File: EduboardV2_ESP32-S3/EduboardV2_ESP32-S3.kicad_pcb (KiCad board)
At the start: 4 copper layers, 35 x 63.3 mm, 22 parts, among them J1 EduboardV2 PCIE UP Board Conn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, Q3 AO3401A, SW1 K2-1102SP-C4SC-04, U1 ESP32-S3-WROOM-1(N8R2), U5 LD1117S33TR_SOT223

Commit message: finish schematic. Do Layout
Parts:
- removed C17: 100n, Capacitor_SMD:C_0603_1608Metric
- removed R19: 10k, Resistor_SMD:R_0603_1608Metric
- removed R29, R30: 0R, Resistor_SMD:R_0603_1608Metric
- added C1: 100n, Capacitor_SMD:C_0603_1608Metric, F.Cu at (133.2, 118.9)
- added C2: 4u7, Capacitor_SMD:C_0805_2012Metric, F.Cu at (133.0, 117.1)
- added C3: 1u, Capacitor_SMD:C_0805_2012Metric, F.Cu at (129.1, 117.5)
- added C4: 4u7, Capacitor_SMD:C_0805_2012Metric, F.Cu at (117.4, 111.2)
- added C5: 100n, Capacitor_SMD:C_0603_1608Metric, F.Cu at (119.2, 111.5)
- added C6: 1u, Capacitor_SMD:C_0805_2012Metric, F.Cu at (117.4, 114.7)
- added JP1: SolderJumper_2_Bridged, Jumper:SolderJumper-2_P1.3mm_Bridged_RoundedPad1.0x1.5mm, B.Cu at (122.1, 137.9)
- added JP10: SolderJumper_3_Bridged12, EduboardV2_kicadlib:SolderJumper_Small-3_bridged12, B.Cu at (127.0, 141.3)
- added JP11: SolderJumper_3_Bridged12, EduboardV2_kicadlib:SolderJumper_Small-3_bridged12, B.Cu at (120.8, 141.3)
- added JP12: SolderJumper_3_Bridged12, EduboardV2_kicadlib:SolderJumper_Small-3_bridged12, B.Cu at (117.7, 141.3)
- added JP2: SolderJumper_2_Bridged, Jumper:SolderJumper-2_P1.3mm_Bridged_RoundedPad1.0x1.5mm, B.Cu at (119.5, 137.9)
- added JP3: SolderJumper_2_Bridged, Jumper:SolderJumper-2_P1.3mm_Bridged_RoundedPad1.0x1.5mm, B.Cu at (116.9, 137.9)
- added JP4: SolderJumper_3_Bridged12, EduboardV2_kicadlib:SolderJumper_Small-3_bridged12, B.Cu at (123.9, 141.3)
- added JP5: SolderJumper_3_Bridged12, EduboardV2_kicadlib:SolderJumper_Small-3_bridged12, B.Cu at (130.8, 124.2)
- added JP6: SolderJumper_3_Bridged12, EduboardV2_kicadlib:SolderJumper_Small-3_bridged12, B.Cu at (133.9, 124.2)
- added JP7: SolderJumper_3_Bridged12, EduboardV2_kicadlib:SolderJumper_Small-3_bridged12, B.Cu at (127.7, 124.2)
- added JP8: SolderJumper_3_Bridged12, EduboardV2_kicadlib:SolderJumper_Small-3_bridged12, B.Cu at (124.6, 124.2)
- added JP9: SolderJumper_3_Bridged12, EduboardV2_kicadlib:SolderJumper_Small-3_bridged12, B.Cu at (130.1, 141.3)
- added Q1: L8050QLT1G, EduboardV2_kicadlib:SOT-23-3_L2.9-W1.3-P1.90-LS2.4-BR, F.Cu at (110.6, 123.9)
- added Q2: L8050QLT1G, EduboardV2_kicadlib:SOT-23-3_L2.9-W1.3-P1.90-LS2.4-BR, F.Cu at (110.6, 120.2)
- added R1: 2k2, Resistor_SMD:R_0402_1005Metric, F.Cu at (119.0, 116.5)
- added R10: 0R, Resistor_SMD:R_0402_1005Metric, F.Cu at (129.0, 115.0)
- added R11: 10k, Resistor_SMD:R_0402_1005Metric, F.Cu at (112.9, 122.4)
- added R12: 10k, Resistor_SMD:R_0402_1005Metric, F.Cu at (112.9, 119.3)
- added R13: 0R, Resistor_SMD:R_0402_1005Metric, F.Cu at (108.3, 124.0)
- added R14: 0R, Resistor_SMD:R_0402_1005Metric, F.Cu at (108.3, 121.2)
- added R2: 10k, Resistor_SMD:R_0402_1005Metric, F.Cu at (130.7, 118.2)
- added R3: 22k, Resistor_SMD:R_0402_1005Metric, F.Cu at (115.4, 115.7)
- added R4: 47k, Resistor_SMD:R_0402_1005Metric, F.Cu at (119.0, 114.0)
- added R8: 10k, Resistor_SMD:R_0402_1005Metric, F.Cu at (120.0, 116.5)
- added R9: 0R, Resistor_SMD:R_0402_1005Metric, F.Cu at (129.0, 114.0)
- added SW2: K2-1102SP-C4SC-04, EduboardV2_kicadlib:KEY-SMD_4P-L6.0-W6.0-P4.50-LS9.5-BL, F.Cu at (104.7, 116.5)
- added U2: CP2102N-A02-GQFN28R, EduboardV2_kicadlib:QFN-28_L5.0-W5.0-P0.50-TL-EP3.3, F.Cu at (123.6, 114.8)
- R25, R31, R32, R6, R7: footprint Resistor_SMD:R_0603_1608Metric -> Resistor_SMD:R_0402_1005Metric
- moved SW1 65.6 mm to (104.7, 128.7), turned to 180 degrees
- moved C27 51.5 mm to (108.2, 108.6), turned to 90 degrees
- moved Q3 47.3 mm to (111.1, 108.9), turned to -90 degrees
- moved C25 44.1 mm to (115.0, 99.4), turned to 90 degrees
- moved U5 43.2 mm to (107.8, 103.2), turned to 180 degrees
- moved D1 41.1 mm to (116.8, 99.2), turned to 90 degrees
- moved C28 38.0 mm to (106.4, 108.6), turned to 90 degrees
- moved D3 35.0 mm to (122.4, 107.5)
- moved R25 33.9 mm to (109.7, 111.3), turned to 180 degrees
- moved D2 32.2 mm to (124.9, 107.5), turned to 180 degrees
- moved C26 30.3 mm to (113.2, 99.4), turned to 90 degrees
- moved USBC1 27.6 mm to (123.6, 98.4), turned to 180 degrees
- moved R6 22.3 mm to (121.1, 103.0), turned to 180 degrees
- moved R31 21.2 mm to (123.1, 109.2), turned to -90 degrees
- moved R32 21.2 mm to (124.1, 109.2), turned to -90 degrees
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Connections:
- J1 pad 10: USB_Debug_D- -> ESP_D-
- J1 pad 11: unconnected-(J1-UART0_UP_RX-Pad11) -> ESP_U1_RX
- J1 pad 12: USB_Debug_D+ -> ESP_D+
- J1 pad 13: unconnected-(J1-UART1_RS485_TX-Pad13) -> ESP_U2_TX
- J1 pad 15: unconnected-(J1-UART1_RS485_RX-Pad15) -> ESP_U2_RX
- J1 pad 16: unconnected-(J1-RS485_DE-Pad16) -> GPIO_RS485_DE
- J1 pad 17: unconnected-(J1-~{FLASH_CS}-Pad17) -> GPIO_FLASH_CS
- J1 pad 18: unconnected-(J1-~{General_Reset}-Pad18) -> ~{GPIO_General_Reset}
- J1 pad 19: unconnected-(J1-~{SD_CS}-Pad19) -> GPIO_SD_CS
- J1 pad 20: unconnected-(J1-~{TFT_CS}-Pad20) -> GPIO_TFT_CS
- J1 pad 22: unconnected-(J1-TFT_DC-Pad22) -> GPIO_TFT_DC
- J1 pad 24: unconnected-(J1-SPI_SCK-Pad24) -> GPIO_SCK
- J1 pad 26: unconnected-(J1-SPI_MISO-Pad26) -> GPIO_MISO
- J1 pad 28: unconnected-(J1-SPI_MOSI-Pad28) -> GPIO_MOSI
- J1 pad 29: unconnected-(J1-WS2812_Data-Pad29) -> GPIO_WS2812_Data
- J1 pad 30: unconnected-(J1-SCL-Pad30) -> GPIO_SCL
- J1 pad 32: unconnected-(J1-SDA-Pad32) -> GPIO_SDA
- J1 pad 34: unconnected-(J1-GPIOX4/AN5/I2S_MCLK-Pad34) -> ESP_GPIO0
- J1 pad 36: unconnected-(J1-GPIOX3/AN4/I2S_SCLK-Pad36) -> GPIOX3
- J1 pad 38: unconnected-(J1-GPIOX2/AN3/I2S_LRCK-Pad38) -> GPIOX2
- J1 pad 40: unconnected-(J1-GPIOX1/AN2/I2S_DIN-Pad40) -> GPIOX1
- J1 pad 42: unconnected-(J1-GPIOX0/AN1/I2S_DOUT-Pad42) -> GPIOX0
- J1 pad 44: unconnected-(J1-AN0/Pot0-Pad44) -> GPIO_AN0
- J1 pad 46: unconnected-(J1-SW0-Pad46) -> GPIO_SW0
- J1 pad 48: unconnected-(J1-SW1-Pad48) -> GPIO_SW1
- J1 pad 50: unconnected-(J1-SW2-Pad50) -> GPIO_SW2
- J1 pad 52: unconnected-(J1-SW3-Pad52) -> GPIO_SW3
- J1 pad 9: unconnected-(J1-UART0_UP_TX-Pad9) -> ESP_U1_TX
- R31 pad 2: /DebugChip/D_N -> D_N
- R32 pad 2: /DebugChip/D_P -> D_P
- SW1 pad 1: UP_Reset -> ESP_EN
- SW1 pad 2: UP_Reset -> ESP_EN
- U1 pad 1: unconnected-(U1-GND-Pad1) -> GND
- U1 pad 10: unconnected-(U1-IO17-Pad10) -> ESP_U1_TX
- U1 pad 11: unconnected-(U1-IO18-Pad11) -> ESP_U1_RX
- U1 pad 12: unconnected-(U1-IO8-Pad12) -> ~{GPIO_General_Reset}
- U1 pad 13: unconnected-(U1-IO19-Pad13) -> ESP_D-
- U1 pad 14: unconnected-(U1-IO20-Pad14) -> ESP_D+
- U1 pad 15: unconnected-(U1-IO3-Pad15) -> GPIO_FLASH_CS
- U1 pad 16: unconnected-(U1-IO46-Pad16) -> GPIO_Buzzer
- U1 pad 17: unconnected-(U1-IO9-Pad17) -> GPIO_AN0
- U1 pad 18: unconnected-(U1-IO10-Pad18) -> GPIO_SD_CS
- U1 pad 19: unconnected-(U1-IO11-Pad19) -> GPIO_TFT_CS
- U1 pad 2: unconnected-(U1-3V3-Pad2) -> +3V3
- U1 pad 20: unconnected-(U1-IO12-Pad20) -> GPIO_MISO
- U1 pad 21: unconnected-(U1-IO13-Pad21) -> GPIO_MOSI
- U1 pad 22: unconnected-(U1-IO14-Pad22) -> GPIO_SCK
- U1 pad 23: unconnected-(U1-IO21-Pad23) -> GPIO_SW0
- U1 pad 24: unconnected-(U1-IO47-Pad24) -> GPIO_SW1
- U1 pad 25: unconnected-(U1-IO48-Pad25) -> GPIO_SW2
- U1 pad 26: unconnected-(U1-IO45-Pad26) -> GPIO_SW3
- U1 pad 27: unconnected-(U1-IO0-Pad27) -> ESP_GPIO0
- U1 pad 28: unconnected-(U1-IO35-Pad28) -> Net-(JP3-A)
- U1 pad 29: unconnected-(U1-IO36-Pad29) -> Net-(JP2-A)
- U1 pad 3: unconnected-(U1-EN-Pad3) -> ESP_EN
- U1 pad 30: unconnected-(U1-IO37-Pad30) -> Net-(JP1-A)
- U1 pad 31: unconnected-(U1-IO38-Pad31) -> GPIO_LED4
- U1 pad 32: unconnected-(U1-IO39-Pad32) -> ESP_GPIO39
- U1 pad 33: unconnected-(U1-IO40-Pad33) -> ESP_GPIO40
- U1 pad 34: unconnected-(U1-IO41-Pad34) -> ESP_GPIO41
- U1 pad 35: unconnected-(U1-IO42-Pad35) -> GPIO_RS485_DE
- U1 pad 36: unconnected-(U1-RXD0-Pad36) -> ESP_U0_RX
- U1 pad 37: unconnected-(U1-TXD0-Pad37) -> ESP_U0_TX
- U1 pad 38: unconnected-(U1-IO2-Pad38) -> GPIO_SDA
- U1 pad 39: unconnected-(U1-IO1-Pad39) -> GPIO_SCL
- U1 pad 4: unconnected-(U1-IO4-Pad4) -> ESP_GPIO4
- U1 pad 40: unconnected-(U1-GND-Pad40) -> GND
- U1 pad 41: unconnected-(U1-GND-Pad41) -> GND
- U1 pad 5: unconnected-(U1-IO5-Pad5) -> ESP_GPIO5
- U1 pad 6: unconnected-(U1-IO6-Pad6) -> ESP_GPIO6
- U1 pad 7: unconnected-(U1-IO7-Pad7) -> ESP_GPIO7
- U1 pad 8: unconnected-(U1-IO15-Pad8) -> GPIO_WS2812_Data
- U1 pad 9: unconnected-(U1-IO16-Pad9) -> GPIO_TFT_DC
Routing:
- net +3V3: track 0.00 -> 107.0 mm, vias 0 -> 4
- net VBUS: track 0.00 -> 106.6 mm, vias 0 -> 2
- net GND: track 0.00 -> 104.7 mm, vias 0 -> 104
- net ESP_GPIO0: track 0.00 -> 83.3 mm, vias 0 -> 3
- net GPIO_WS2812_Data: track 0.00 -> 67.3 mm, vias 0 -> 2
- net GPIO_TFT_DC: track 0.00 -> 61.9 mm, vias 0 -> 2
- net ~{GPIO_General_Reset}: track 0.00 -> 56.0 mm, vias 0 -> 2
- net 3.3V_Sense: track 0.00 -> 54.5 mm, vias 0 -> 1
- net GPIOX1: track 0.00 -> 49.3 mm, vias 0 -> 2
- net ESP_D-: track 0.00 -> 48.2 mm, vias 0 -> 1
- net ESP_D+: track 0.00 -> 48.1 mm, vias 0 -> 1
- net GPIOX3: track 0.00 -> 47.5 mm, vias 0 -> 2
- net GPIO_AN0: track 0.00 -> 47.2 mm, vias 0 -> 2
- net GPIO_RS485_DE: track 0.00 -> 46.5 mm, vias 0 -> 3
- net GPIOX0: track 0.00 -> 45.3 mm, vias 0 -> 2
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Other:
- board text added: "Eduboard2 UP-Board ESP32-S3 V${HW_VERSION}"
- board text removed: "Eduboard2 UP-Board xxx V${HW_VERSION}"

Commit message: add logo
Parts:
- added G***: LOGO, EduboardV2_kicadlib:logo_opportunity, F.Cu at (109.3, 141.6)
- added G***: LOGO, EduboardV2_kicadlib:logo3, F.Cu at (132.3, 104.4)
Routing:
- net GND: track 104.7 -> 117.5 mm, vias 104 -> 18

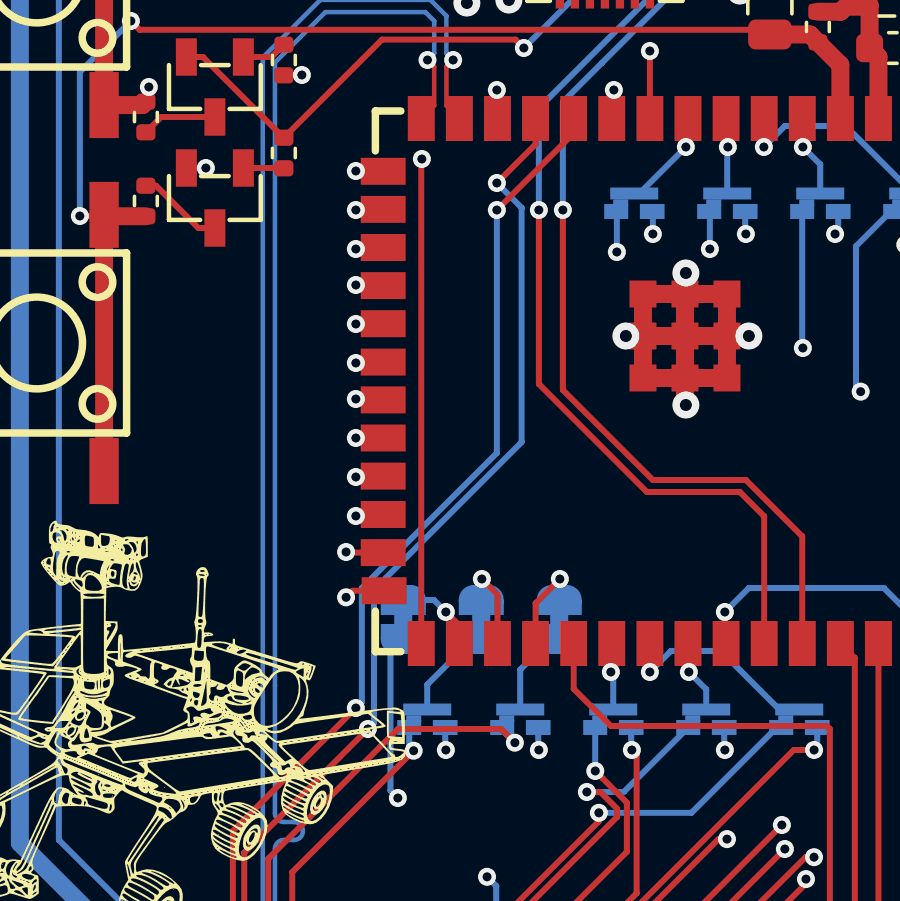
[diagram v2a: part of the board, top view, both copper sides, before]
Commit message: add jumper description on board
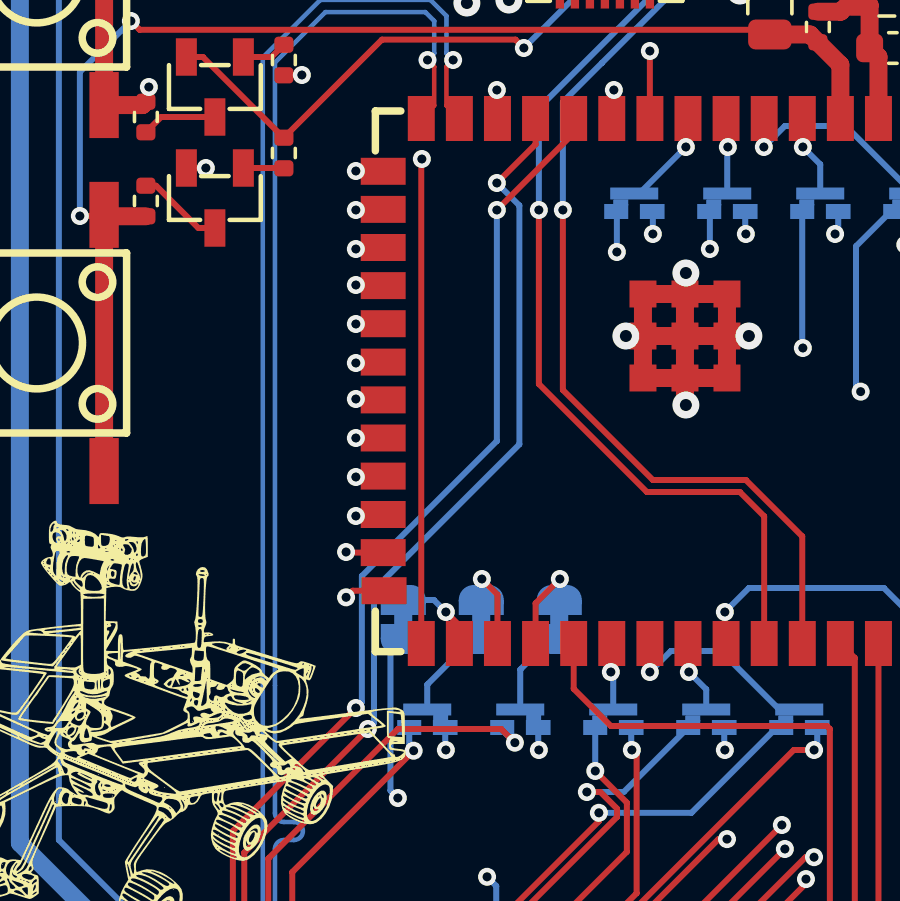
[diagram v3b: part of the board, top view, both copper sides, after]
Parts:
- JP11, JP12: footprint EduboardV2_kicadlib:SolderJumper_Small-3_bridged12 -> EduboardV2_kicadlib:SolderJumper_Small-3_bridged23
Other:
- board text added: "ENC_A PWM_B"
- board text added: "ENC_B PWM_G"
- board text added: "ENC_SW PWM_R"
- board text added: "JP1"
- board text added: "JP2"
- board text added: "JP3"
- board text added: "LED0 GPIOX3"
- board text added: "LED1 GPIOX2"
- board text added: "LED2 GPIOX0"
- board text added: "LED3 GPIOX1"
- board text added: "U2_RX LED7"
- board text added: "U2_TX LED6"
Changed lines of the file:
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@@
       ))
   )
-  (footprint "EduboardV2_kicadlib:SolderJumper_Small-3_bridged12" (layer "B.Cu")
+  (footprint "EduboardV2_kicadlib:SolderJumper_Small-3_bridged23" (layer "B.Cu")
     (at 117.68 141.35)
     (descr "SMD Solder 3-pad Jumper, 1x1.5mm rounded Pads, 0.3mm gap, pads 1-2 bridged with 1 copper strip")
@@
     (attr exclude_from_pos_files)
     (net_tie_pad_groups "1, 2, 3")
-    (fp_text reference "JP12" (at 0 1.8) (layer "B.SilkS") hide
+    (fp_text reference "JP12" (at 0 1.8 180) (layer "B.SilkS") hide
         (effects (font (size 1 1) (thickness 0.15)) (justify mirror))
     )
-    (fp_text value "SolderJumper_3_Bridged12" (at 0 -1.9) (layer "B.Fab") hide
+    (fp_text value "SolderJumper_3_Bridged12" (at 0 -1.9 180) (layer "B.Fab") hide
         (effects (font (size 1 1) (thickness 0.15)) (justify mirror))
     )
     (fp_poly
       (pts
-        (xy -0.7 0)
-        (xy -0.2 0)
-        (xy -0.2 -0.2)
-        (xy -0.7 -0.2)
+        (xy 0.1955 -0.05)
+        (xy 0.6955 -0.05)
+        (xy 0.6955 -0.25)
+        (xy 0.1955 -0.25)
       )
       (stroke (width 0) (type solid)) (fill solid) (layer "B.Cu"))
@@
       (net 28 "GPIOX2") (pinfunction "B") (pintype "passive") (zone_connect 2) (thermal_bridge_angle 45))
   )
-  (footprint "EduboardV2_kicadlib:SolderJumper_Small-3_bridged12" (layer "B.Cu")
+  (footprint "EduboardV2_kicadlib:SolderJumper_Small-3_bridged23" (layer "B.Cu")
     (at 120.78 141.35)
     (descr "SMD Solder 3-pad Jumper, 1x1.5mm rounded Pads, 0.3mm gap, pads 1-2 bridged with 1 copper strip")
@@
     (attr exclude_from_pos_files)
     (net_tie_pad_groups "1, 2, 3")
-    (fp_text reference "JP11" (at 0 1.8) (layer "B.SilkS") hide
+    (fp_text reference "JP11" (at 0 1.8 180) (layer "B.SilkS") hide
         (effects (font (size 1 1) (thickness 0.15)) (justify mirror))
     )
-    (fp_text value "SolderJumper_3_Bridged12" (at 0 -1.9) (layer "B.Fab") hide
+    (fp_text value "SolderJumper_3_Bridged12" (at 0 -1.9 180) (layer "B.Fab") hide
         (effects (font (size 1 1) (thickness 0.15)) (justify mirror))
     )
     (fp_poly
       (pts
-        (xy -0.7 0)
-        (xy -0.2 0)
-        (xy -0.2 -0.2)
-        (xy -0.7 -0.2)
+        (xy 0.1955 -0.05)
+        (xy 0.6955 -0.05)
+        (xy 0.6955 -0.25)
+        (xy 0.1955 -0.25)
       )
       (stroke (width 0) (type solid)) (fill solid) (layer "B.Cu"))
@@
     (pad "3" smd rect (at 0.6 0.2 270) (size 0.5 0.825) (layers "B.Cu" "B.Mask")
       (net 33 "GPIO_PWM_R") (pinfunction "B") (pintype "passive") (zone_connect 2) (thermal_bridge_angle 45))
+  )
+  (gr_text "U2_RX\nLED7" (at 118.75 142.75 90) (layer "B.SilkS")
+    (effects (font (size 0.8 0.8) (thickness 0.2) bold) (justify left bottom mirror))
+  )
+  (gr_text "LED1\nGPIOX2" (at 135 125.5 90) (layer "B.SilkS")
+    (effects (font (size 0.8 0.8) (thickness 0.2) bold) (justify left bottom mirror))
+  )
+  (gr_text "ENC_B\nPWM_G" (at 131 142.75 90) (layer "B.SilkS")
+    (effects (font (size 0.8 0.8) (thickness 0.2) bold) (justify left bottom mirror))
+  )
+  (gr_text "ENC_A\nPWM_B" (at 128 142.75 90) (layer "B.SilkS")
+    (effects (font (size 0.8 0.8) (thickness 0.2) bold) (justify left bottom mirror))
+  )
+  (gr_text "JP2" (at 119 136.25 270) (layer "B.SilkS")
+    (effects (font (size 0.8 0.8) (thickness 0.2) bold) (justify left bottom mirror))
+  )
+  (gr_text "LED0\nGPIOX3" (at 132 125.5 90) (layer "B.SilkS")
+    (effects (font (size 0.8 0.8) (thickness 0.2) bold) (justify left bottom mirror))
+  )
+  (gr_text "JP3" (at 116.5 136.25 270) (layer "B.SilkS")
+    (effects (font (size 0.8 0.8) (thickness 0.2) bold) (justify left bottom mirror))
+  )
+  (gr_text "U2_TX\nLED6" (at 122 142.75 90) (layer "B.SilkS")
+    (effects (font (size 0.8 0.8) (thickness 0.2) bold) (justify left bottom mirror))
+  )
+  (gr_text "LED2\nGPIOX0" (at 129 125.5 90) (layer "B.SilkS")
+    (effects (font (size 0.8 0.8) (thickness 0.2) bold) (justify left bottom mirror))
+  )
+  (gr_text "LED3\nGPIOX1" (at 125.75 125.5 90) (layer "B.SilkS")
+    (effects (font (size 0.8 0.8) (thickness 0.2) bold) (justify left bottom mirror))
+  )
+  (gr_text "ENC_SW\nPWM_R" (at 125 142.75 90) (layer "B.SilkS")
+    (effects (font (size 0.8 0.8) (thickness 0.2) bold) (justify left bottom mirror))
+  )
+  (gr_text "JP1" (at 121.5 136.25 270) (layer "B.SilkS")
+    (effects (font (size 0.8 0.8) (thickness 0.2) bold) (justify left bottom mirror))
   )
   (gr_text "Eduboard2\nUP-Board ESP32-S3 V${HW_VERSION}" (at 110.2 151.7) (layer "F.SilkS")
@@
   (via (at 115.3 140.9) (size 0.6) (drill 0.3) (layers "F.Cu" "B.Cu") (net 5))
   (via (at 120 124.3) (size 0.6) (drill 0.3) (layers "F.Cu" "B.Cu") (net 5))
-  (segment (start 120 132.4) (end 115.5 136.9) (width 0.2) (layer "B.Cu") (net 5))
+  (segment (start 115.5 136.5) (end 115.5 140.7) (width 0.2) (layer "B.Cu") (net 5))
+  (segment (start 120 124.3) (end 120 132) (width 0.2) (layer "B.Cu") (net 5))
+  (segment (start 120 132) (end 115.5 136.5) (width 0.2) (layer "B.Cu") (net 5))
   (segment (start 115.5 140.7) (end 115.3 140.9) (width 0.2) (layer "B.Cu") (net 5))
-  (segment (start 115.5 136.9) (end 115.5 140.7) (width 0.2) (layer "B.Cu") (net 5))
-  (segment (start 120 124.3) (end 120 132.4) (width 0.2) (layer "B.Cu") (net 5))
   (segment (start 118.75 121.25) (end 118.318201 120.818201) (width 0.1524) (layer "F.Cu") (net 6))
   (segment (start 118.318201 119.523799) (end 118.542 119.3) (width 0.1524) (layer "F.Cu") (net 6))
@@
   (via (at 115.7 141.6) (size 0.6) (drill 0.3) (layers "F.Cu" "B.Cu") (net 7))
   (via (at 120 123.4) (size 0.6) (drill 0.3) (layers "F.Cu" "B.Cu") (net 7))
+  (segment (start 115.903 136.958742) (end 120.75 132.111742) (width 0.2) (layer "B.Cu") (net 7))
+  (segment (start 120.75 132.111742) (end 120.75 124.15) (width 0.2) (layer "B.Cu") (net 7))
+  (segment (start 115.903 141.397) (end 115.903 136.958742) (width 0.2) (layer "B.Cu") (net 7))
   (segment (start 115.7 141.6) (end 115.903 141.397) (width 0.2) (layer "B.Cu") (net 7))
-  (segment (start 120.8265 132.035242) (end 120.8265 124.2265) (width 0.2) (layer "B.Cu") (net 7))
-  (segment (start 115.903 136.958742) (end 120.8265 132.035242) (width 0.2) (layer "B.Cu") (net 7))
-  (segment (start 120.8265 124.2265) (end 120 123.4) (width 0.2) (layer "B.Cu") (net 7))
-  (segment (start 115.903 141.397) (end 115.903 136.958742) (width 0.2) (layer "B.Cu") (net 7))
+  (segment (start 120.75 124.15) (end 120 123.4) (width 0.2) (layer "B.Cu") (net 7))
   (segment (start 117.911799 120.818201) (end 117.911799 119.523799) (width 0.1524) (layer "F.Cu") (net 8))
   (segment (start 117.48 121.25) (end 117.911799 120.818201) (width 0.1524) (layer "F.Cu") (net 8))
